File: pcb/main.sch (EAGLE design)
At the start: 20 parts, among them IC1 FT230XS, J3 455-1750-1-ND, Q1 2.5A/30V/105mΩ

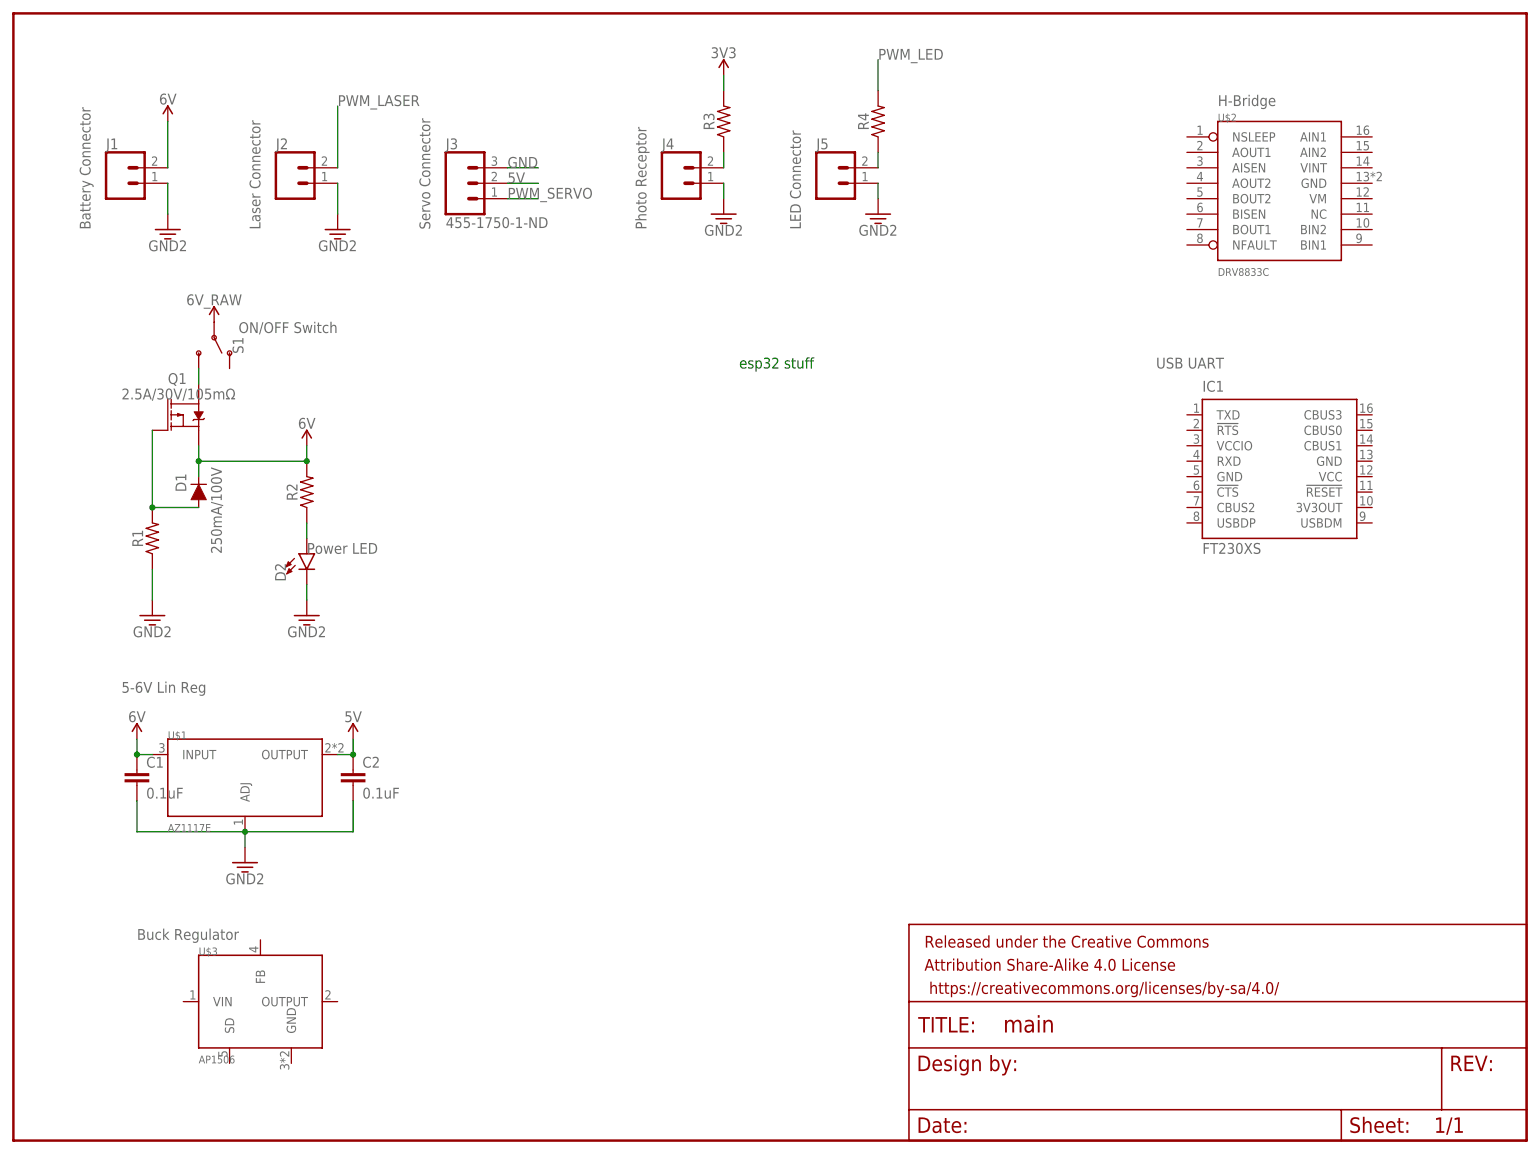
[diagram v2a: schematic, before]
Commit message: finished hbridge and buck converter
created part for inductor, figured out values for buck converter caps,
and wired hbridge
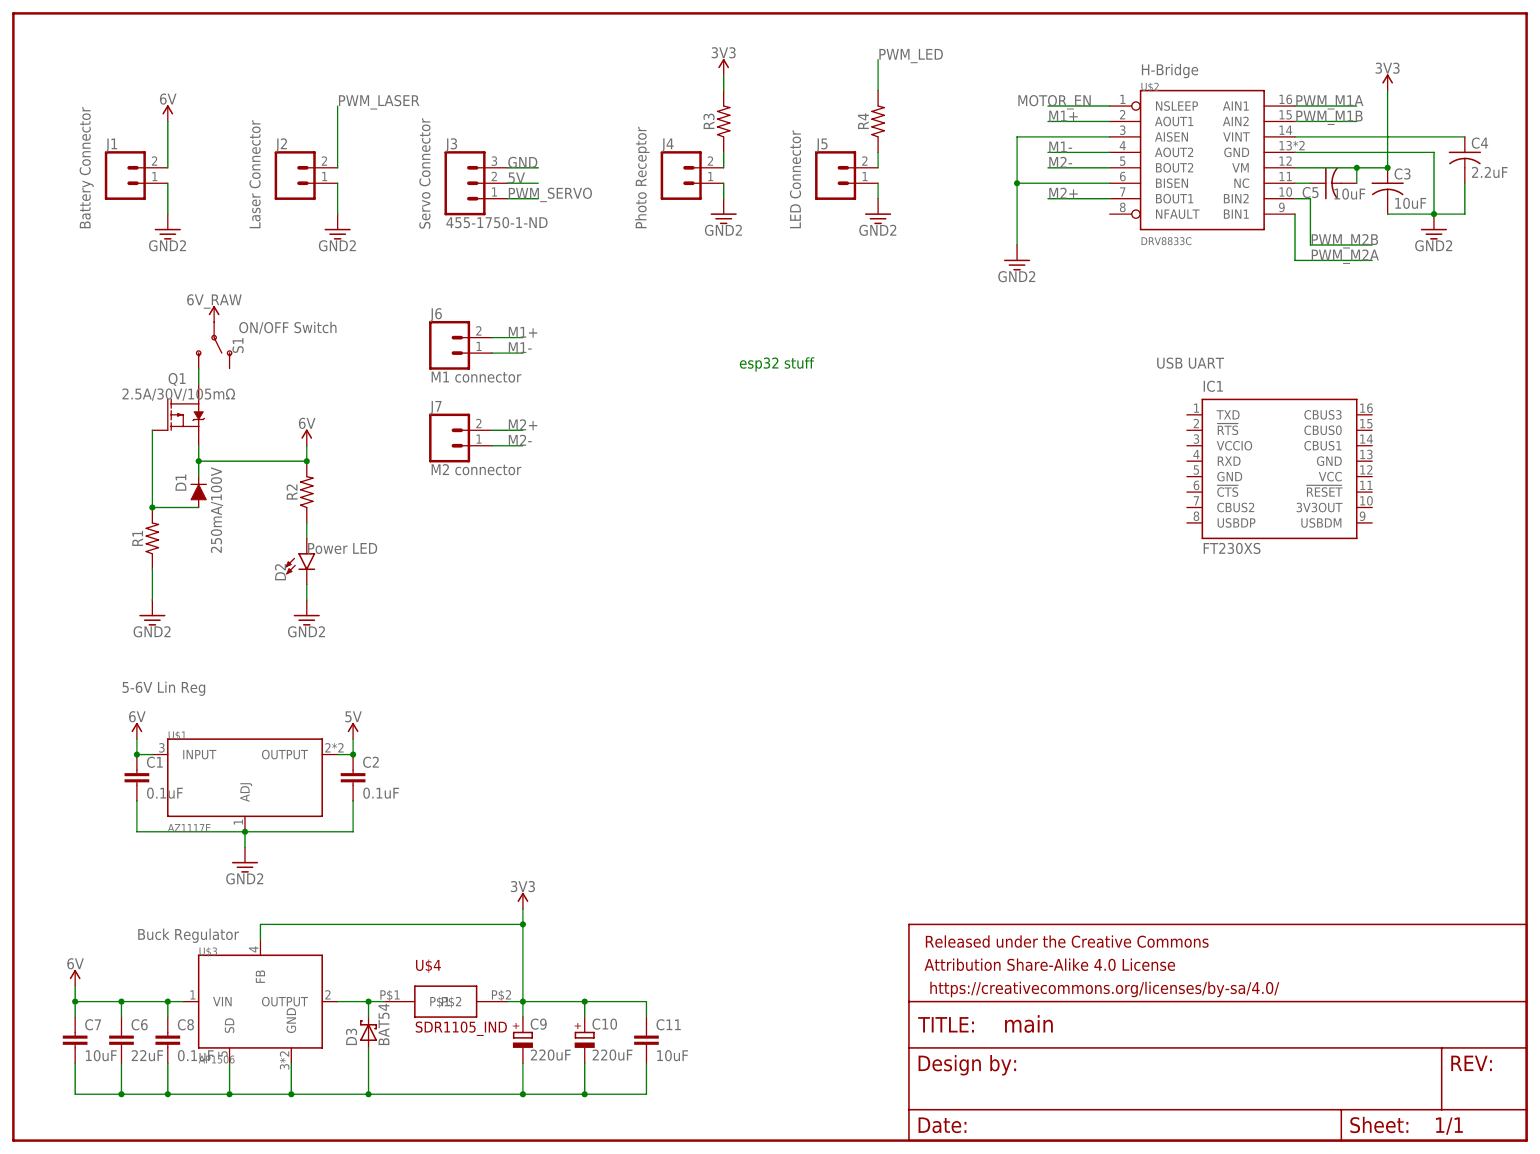
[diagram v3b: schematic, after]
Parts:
- added C10, C9: 220uF, rcl:CPOL-EUB/3528-21R
- added C11, C7: 10uF, rcl:C-EUC0805
- added C3, C5: 10uF, rcl:C-USC0603
- added C4: 2.2uF, rcl:C-USC0603
- added C6: 22uF, rcl:C-EUC0805
- added C8: 0.1uF, electricSheepParty:0.1UF-0603-25V-(+80/-20%)
- added D3: BAT54, diode:BAT54
- added J6: M1 connector, electricSheepParty:CONN_02
- added J7: M2 connector, electricSheepParty:CONN_02
- added U$4: SDR1105_IND, sheep:SDR1105_IND
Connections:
- removed net 3.3V: C1.2, C2.2, D2.C, J1.1, J2.1, J4.1, J5.1, R1.1, U$1.ADJ
- new net 3V3: C10.+, C11.1, C3.1, C5.2, C9.+, R3.2, U$2.VM, U$3.FB, U$4.P$2
- new net 6V: C1.1, C6.1, C7.1, C8.1, U$1.INPUT, U$3.VIN
- new net M1+: J6.2, U$2.AOUT1
- new net M1-: J6.1, U$2.AOUT2
- new net M2+: J7.2, U$2.BOUT1
- new net M2-: J7.1, U$2.BOUT2
- new net MOTOR_EN: U$2.NSLEEP
- new net N$10: C10.-, C11.2, C6.2, C7.2, C8.2, C9.-, D3.A, U$3.GND, U$3.SD
- new net N$6: C3.2, C4.2, U$2.GND
- new net N$7: D3.C, U$3.OUTPUT, U$4.P$1
- new net N$8: C4.1, U$2.VINT
- new net N$9: C5.1, U$2.NC
- new net PWM_M1A: U$2.AIN1
- new net PWM_M1B: U$2.AIN2
- new net PWM_M2A: U$2.BIN1
- new net PWM_M2B: U$2.BIN2
- net 5V: now also C2.1, U$1.OUTPUT
- net GND: now also C1.2, C2.2, D2.C, J1.1, J2.1, J4.1, J5.1, R1.1, U$1.ADJ, U$2.AISEN, U$2.BISEN
- net VCC: no longer C1.1, C2.1, R3.2, U$1.INPUT, U$1.OUTPUT
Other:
- moved on the sheet: U$2

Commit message: updated hbridge
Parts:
- added R5: (no value), electricSheepParty:RESISTOR0603
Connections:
- removed net MOTOR_EN: U$2.NSLEEP
- new net N$13: R5.1, U$2.NFAULT
- net 3V3: now also R5.2, U$2.NSLEEP
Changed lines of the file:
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@@
 <part name="C10" library="rcl" library_urn="urn:adsk.eagle:library:334" deviceset="CPOL-EU" device="B/3528-21R" package3d_urn="urn:adsk.eagle:package:23409/2" value="220uF"/>
 <part name="C11" library="rcl" library_urn="urn:adsk.eagle:library:334" deviceset="C-EU" device="C0805" package3d_urn="urn:adsk.eagle:package:23617/2" value="10uF"/>
+<part name="R5" library="electricSheepParty" deviceset="RESISTOR" device="0603" value=" "/>
 </parts>
 <sheets>
@@
 <attribute name="VALUE" x="1258.824" y="118.491" size="1.778" layer="96" rot="R180"/>
 </instance>
-<instance part="GND9" gate="G$1" x="1201.42" y="106.68"/>
+<instance part="GND9" gate="G$1" x="1191.26" y="106.68"/>
 <instance part="J6" gate="G$1" x="1107.44" y="91.44"/>
 <instance part="J7" gate="G$1" x="1107.44" y="76.2"/>
@@
 <instance part="C10" gate="G$1" x="1130.3" y="-20.32"/>
 <instance part="C11" gate="G$1" x="1140.46" y="-20.32"/>
+<instance part="R5" gate="G$1" x="1209.04" y="114.3" rot="R180"/>
 </instances>
 <busses>
@@
 <segment>
 <pinref part="U$2" gate="G$1" pin="BISEN"/>
-<wire x1="1216.66" y1="119.38" x2="1201.42" y2="119.38" width="0.1524" layer="91"/>
-<wire x1="1201.42" y1="119.38" x2="1201.42" y2="127" width="0.1524" layer="91"/>
+<wire x1="1216.66" y1="119.38" x2="1191.26" y2="119.38" width="0.1524" layer="91"/>
+<wire x1="1191.26" y1="119.38" x2="1191.26" y2="127" width="0.1524" layer="91"/>
 <pinref part="U$2" gate="G$1" pin="AISEN"/>
-<wire x1="1201.42" y1="127" x2="1216.66" y2="127" width="0.1524" layer="91"/>
+<wire x1="1191.26" y1="127" x2="1216.66" y2="127" width="0.1524" layer="91"/>
 <pinref part="GND9" gate="G$1" pin="3.3V"/>
-<wire x1="1201.42" y1="109.22" x2="1201.42" y2="119.38" width="0.1524" layer="91"/>
-<junction x="1201.42" y="119.38"/>
+<wire x1="1191.26" y1="109.22" x2="1191.26" y2="119.38" width="0.1524" layer="91"/>
+<junction x="1191.26" y="119.38"/>
 </segment>
 </net>
@@
 <junction x="1130.3" y="-15.24"/>
 </segment>
+<segment>
+<pinref part="R5" gate="G$1" pin="2"/>
+<wire x1="1203.96" y1="114.3" x2="1196.34" y2="114.3" width="0.1524" layer="91"/>
+<label x="1196.34" y="114.3" size="1.778" layer="95"/>
+</segment>
+<segment>
+<pinref part="U$2" gate="G$1" pin="NSLEEP"/>
+<wire x1="1216.66" y1="132.08" x2="1206.5" y2="132.08" width="0.1524" layer="91"/>
+<label x="1206.5" y="132.08" size="1.778" layer="95"/>
+</segment>
 </net>
 <net name="N$8" class="0">
@@
 <wire x1="1249.68" y1="109.22" x2="1259.84" y2="109.22" width="0.1524" layer="91"/>
 <label x="1249.68" y="109.22" size="1.778" layer="95"/>
-</segment>
-</net>
-<net name="MOTOR_EN" class="0">
-<segment>
-<pinref part="U$2" gate="G$1" pin="NSLEEP"/>
-<wire x1="1216.66" y1="132.08" x2="1206.5" y2="132.08" width="0.1524" layer="91"/>
-<label x="1201.42" y="132.08" size="1.778" layer="95"/>
 </segment>
 </net>
@@
 </segment>
 </net>
+<net name="N$13" class="0">
+<segment>
+<pinref part="U$2" gate="G$1" pin="NFAULT"/>
+<pinref part="R5" gate="G$1" pin="1"/>
+<wire x1="1216.66" y1="114.3" x2="1214.12" y2="114.3" width="0.1524" layer="91"/>
+</segment>
+</net>

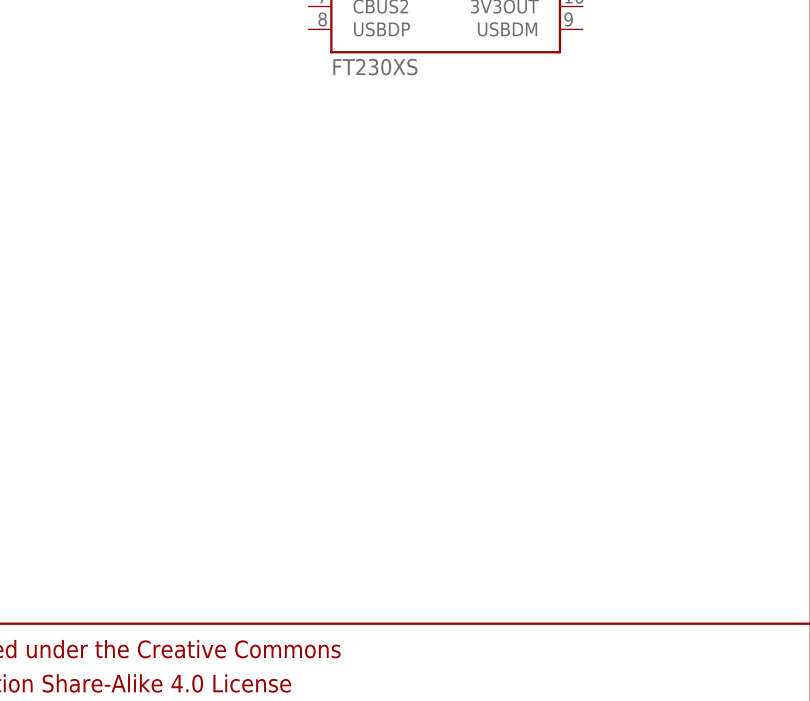
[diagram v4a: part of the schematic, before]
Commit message: added IMU
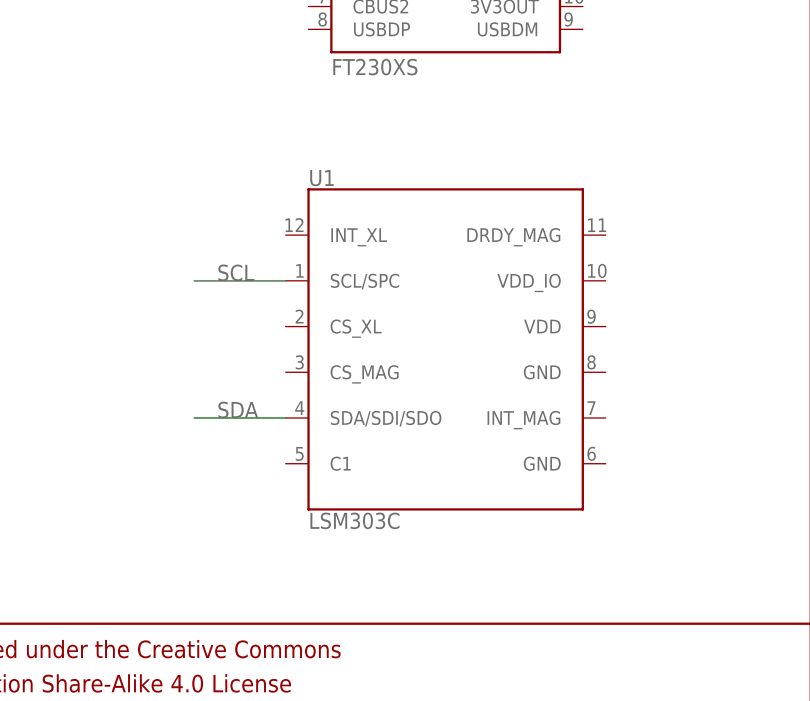
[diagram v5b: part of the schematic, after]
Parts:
- added U1: LSM303C, SparkFun-Sensors:LSM303C
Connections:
- new net SCL: U1.SCL/SPC
- new net SDA: U1.SDA/SDI/SDO
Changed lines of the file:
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@@
 <part name="C11" library="rcl" library_urn="urn:adsk.eagle:library:334" deviceset="C-EU" device="C0805" package3d_urn="urn:adsk.eagle:package:23617/2" value="10uF"/>
 <part name="R5" library="electricSheepParty" deviceset="RESISTOR" device="0603" value=" "/>
+<part name="U1" library="SparkFun-Sensors" library_urn="urn:adsk.eagle:library:534" deviceset="LSM303C" device="" package3d_urn="urn:adsk.eagle:package:39983/1" value="LSM303C"/>
 </parts>
 <sheets>
@@
 <instance part="C11" gate="G$1" x="1140.46" y="-20.32"/>
 <instance part="R5" gate="G$1" x="1209.04" y="114.3" rot="R180"/>
+<instance part="U1" gate="G$1" x="1244.6" y="27.94"/>
 </instances>
 <busses>
@@
 </segment>
 </net>
+<net name="SCL" class="0">
+<segment>
+<pinref part="U1" gate="G$1" pin="SCL/SPC"/>
+<wire x1="1226.82" y1="35.56" x2="1216.66" y2="35.56" width="0.1524" layer="91"/>
+<label x="1219.2" y="35.56" size="1.778" layer="95"/>
+</segment>
+</net>
+<net name="SDA" class="0">
+<segment>
+<pinref part="U1" gate="G$1" pin="SDA/SDI/SDO"/>
+<wire x1="1226.82" y1="20.32" x2="1216.66" y2="20.32" width="0.1524" layer="91"/>
+<label x="1219.2" y="20.32" size="1.778" layer="95"/>
+</segment>
+</net>

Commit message: changed gnd symbol (some weird 3.3v thing was happening) and added esp32
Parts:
- added U2: ESP-WROOM-32, electricSheepParty:ESP-WROOM-32
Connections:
- removed net N$10: C10.-, C11.2, C6.2, C7.2, C8.2, C9.-, D3.A, U$3.GND, U$3.SD
- removed net N$6: C3.2, C4.2, U$2.GND
- net GND: now also C10.-, C11.2, C3.2, C4.2, C6.2, C7.2, C8.2, C9.-, D3.A, U$2.GND, U$3.GND, U$3.SD, U2.GND@1, U2.GND@3
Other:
- note removed: "esp32 stuff"
- moved on the sheet: C1, C10, C11, C2, C3, C4, C5, C6, C7, C8, C9, D1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

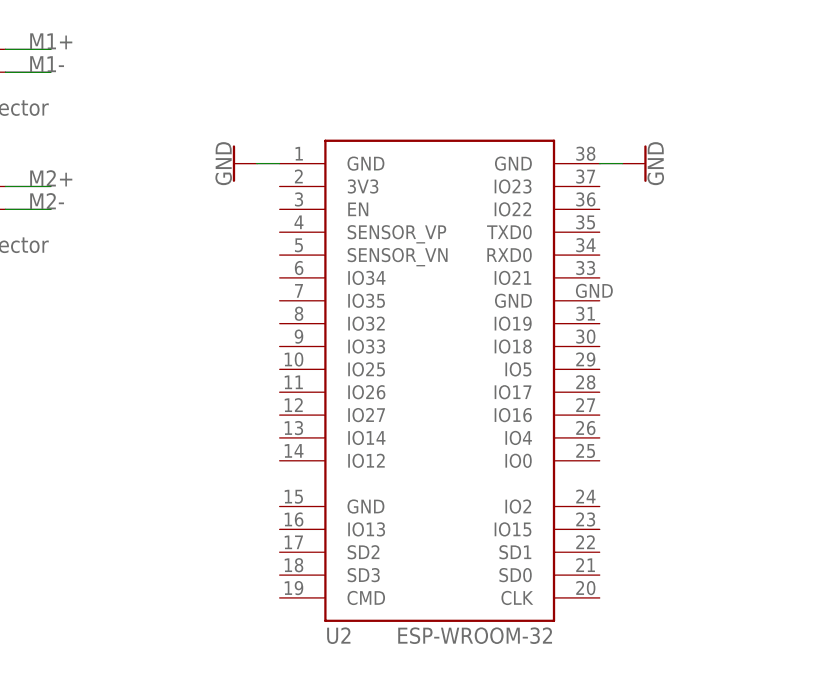
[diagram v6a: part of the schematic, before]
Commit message: added in new gnd symbols (doesn't default to 3.3v anymore); added in esp32 library
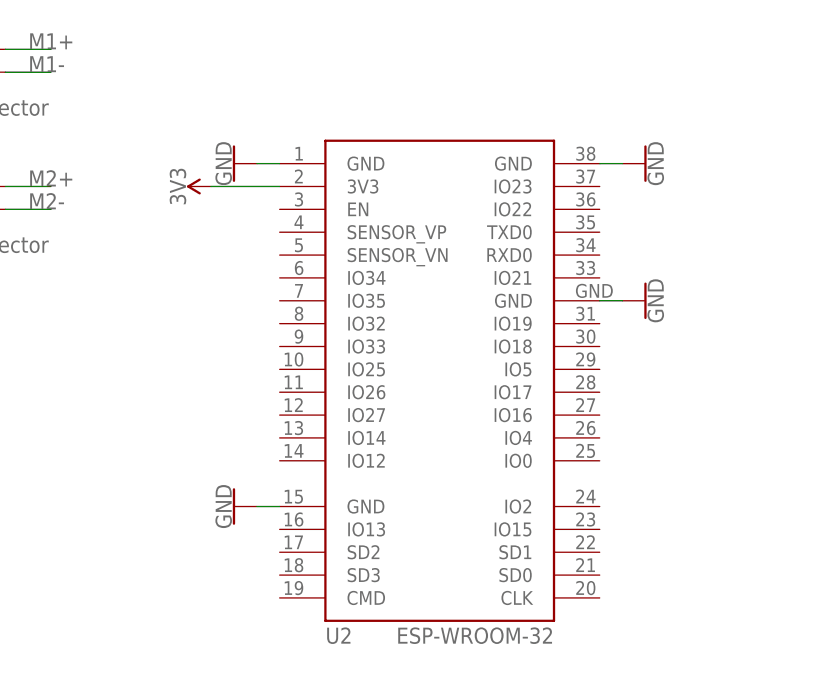
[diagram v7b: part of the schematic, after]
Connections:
- net GND: now also U2.GND@2, U2.GND@4
- net VCC: now also U2.3V3
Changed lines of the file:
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@@
 <part name="GND7" library="SparkFun-PowerSymbols" deviceset="GND" device=""/>
 <part name="GND10" library="SparkFun-PowerSymbols" deviceset="GND" device=""/>
+<part name="GND12" library="SparkFun-PowerSymbols" deviceset="GND" device=""/>
+<part name="GND13" library="SparkFun-PowerSymbols" deviceset="GND" device=""/>
+<part name="SUPPLY10" library="SparkFun-PowerSymbols" deviceset="VCC" device="" value="3V3"/>
 </parts>
 <sheets>
@@
 <instance part="GND7" gate="1" x="10.16" y="5.08"/>
 <instance part="GND10" gate="1" x="149.86" y="119.38" rot="R90"/>
+<instance part="GND12" gate="1" x="149.86" y="104.14" rot="R90"/>
+<instance part="GND13" gate="1" x="104.14" y="81.28" rot="R270"/>
+<instance part="SUPPLY10" gate="G$1" x="101.6" y="116.84" rot="R90"/>
 </instances>
 <busses>
@@
 <pinref part="S1" gate="1" pin="P"/>
 <pinref part="SUPPLY3" gate="G$1" pin="VCC"/>
+</segment>
+<segment>
+<pinref part="U2" gate="G$1" pin="3V3"/>
+<pinref part="SUPPLY10" gate="G$1" pin="VCC"/>
+<wire x1="101.6" y1="116.84" x2="109.22" y2="116.84" width="0.1524" layer="91"/>
 </segment>
 </net>
@@
 <junction x="10.16" y="7.62"/>
 </segment>
+<segment>
+<pinref part="U2" gate="G$1" pin="GND@4"/>
+<pinref part="GND12" gate="1" pin="GND"/>
+<wire x1="147.32" y1="104.14" x2="144.78" y2="104.14" width="0.1524" layer="91"/>
+</segment>
+<segment>
+<pinref part="U2" gate="G$1" pin="GND@2"/>
+<pinref part="GND13" gate="1" pin="GND"/>
+<wire x1="106.68" y1="81.28" x2="109.22" y2="81.28" width="0.1524" layer="91"/>
+</segment>
 </net>

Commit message: Did IMU and most of UART
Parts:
- added C12, C13: 0.1uF, electricSheepParty:0.1UF-0603-25V-(+80/-20%)
- added C14: 10uF, electricSheepParty:0.1UF-0603-25V-(+80/-20%)
- added CN1: (no value), adafruit:USBMINIB
- added FRAME2: FRAME-LETTERNO_PACKAGE, SparkFun-Aesthetics:FRAME-LETTERNO_PACKAGE
- added J8: (no value), electricSheepParty:CONN_02
- added R6, R7: 10k, electricSheepParty:RESISTOR0603
- added RESET: SWITCH, DiscreteComponents:SWITCH
- R1: value (none) -> 100k
- R2: value (none) -> 330
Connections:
- new net CTS: IC1.!CTS
- new net D+: CN1.D+, IC1.USBDP
- new net D-: CN1.D-, IC1.USBDM
- new net INT_MAG: J8.1, U1.INT_MAG
- new net INT_XL: J8.2, U1.INT_XL
- new net MAG_RDY: U1.DRDY_MAG
- new net N$12: R6.2, R7.1, U1.CS_MAG, U1.CS_XL
- new net N$6: C12.1, U1.C1
- new net RESET: IC1.!RESET, RESET.P$1
- new net RTS: IC1.!RTS
- new net RX: IC1.RXD
- new net TX: IC1.TXD
- net 3V3: now also C13.1, C14.1, CN1.VBUS, IC1.3V3OUT, IC1.VCC, IC1.VCCIO, R7.2, U1.VDD, U1.VDD_IO, U2.3V3
- net GND: now also C12.2, C13.2, C14.2, CN1.GND, IC1.GND, IC1.GND@1, R6.1, RESET.P$2, U1.GND@1, U1.GND@2
- net VCC: no longer U2.3V3
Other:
- note added: "IMU"
- note added: "high for I2C"
- note added: "low for SPI"
- moved on the sheet: U1
